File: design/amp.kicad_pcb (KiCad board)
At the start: 2 copper layers, 61 x 36 mm, 59 parts, among them IC1 CP2102N-A02-GQFN24R, IC2 STM6601CQ2BDM6F, IC3 LD39200PU33R, J1 USB4105-GF-A, J2 SM04B-SRSS-TB(LF)(SN), J3 Conn_01x02_Female, J4 Conn_02x03_Odd_Even, J5 SM04B-SRSS-TB(LF)(SN), J6 SM04B-SRSS-TB(LF)(SN), J7 SM04B-SRSS-TB(LF)(SN), Q1 PMBT2222,215, Q2 PMBT2222,215, Q3 Si2347DS-T1-GE3, U1 ESP32-WROOM-32D, U2 LIS2HH12

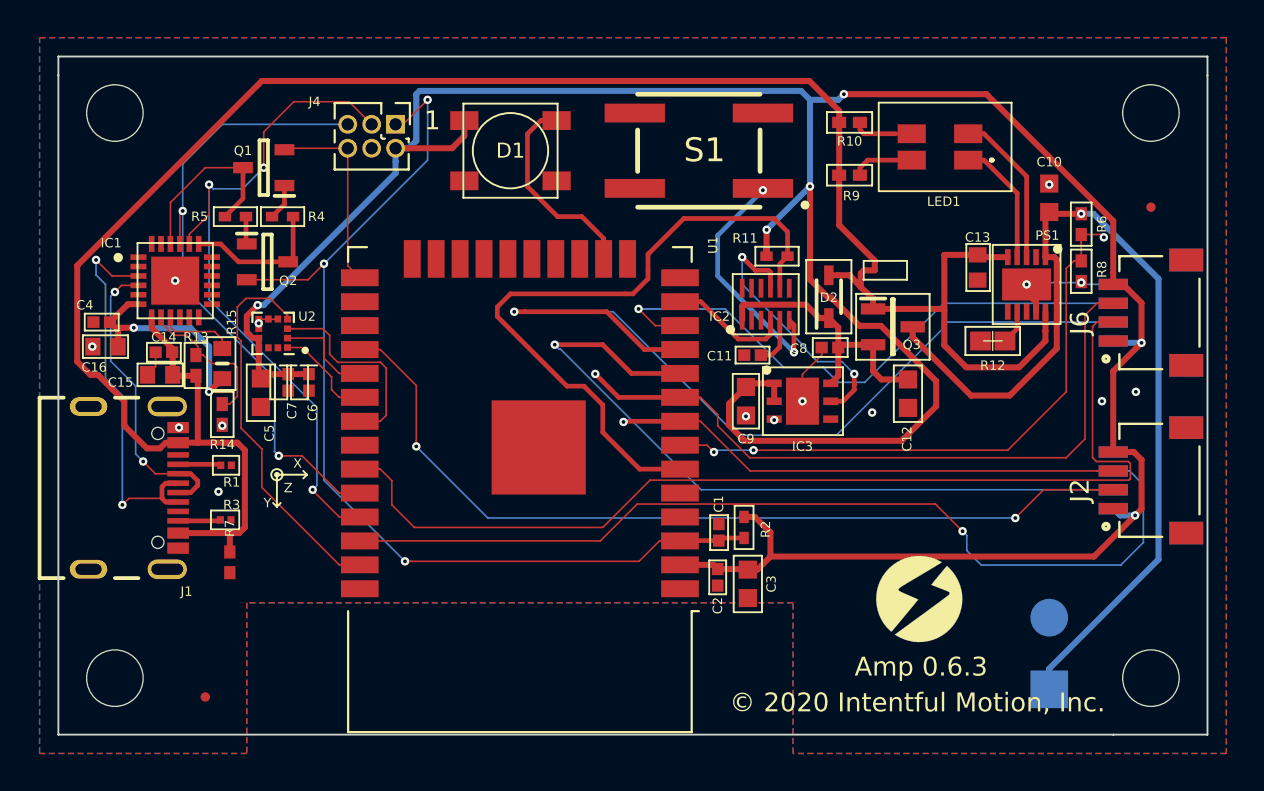
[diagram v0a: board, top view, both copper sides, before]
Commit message: moved components to fit all connectors on the top layer
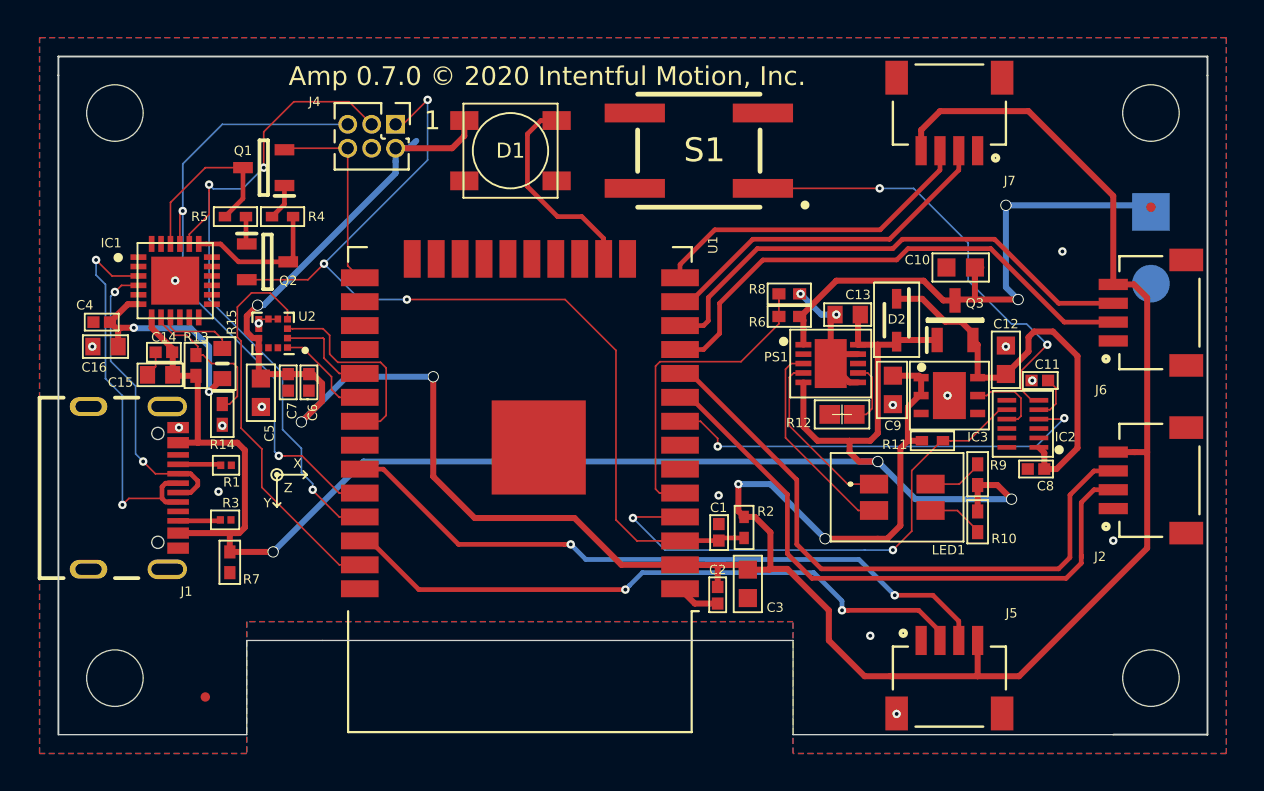
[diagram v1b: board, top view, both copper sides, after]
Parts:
- removed the G*** at (100.7, 60.8)
- J5, J7: moved to F.Cu
- moved J3 25.9 mm to (113.0, 40.2), turned to 270 degrees
- moved R10 22.3 mm to (103.8, 56.7), turned to 90 degrees
- moved LED1 18.7 mm to (99.8, 55.4), turned to 0 degrees
- moved R9 17.3 mm to (103.8, 54.2), turned to 270 degrees
- moved R6 16.3 mm to (93.8, 45.8), turned to 0 degrees
- moved R8 15.5 mm to (93.8, 44.6), turned to 0 degrees
- moved C11 15.3 mm to (107.1, 49.2)
- moved IC2 15.1 mm to (106.2, 51.5), turned to 180 degrees
- moved R11 12.8 mm to (101.4, 52.4)
- moved C8 12.7 mm to (106.9, 53.9)
- moved J7 12.2 mm to (102.3, 37.0), turned to 180 degrees
- moved J5 12.2 mm to (102.3, 63.0), turned to 0 degrees
- moved PS1 11.2 mm to (96.0, 48.3), turned to 0 degrees
- moved R12 8.90 mm to (96.6, 51.0)
- moved C9 7.82 mm to (99.3, 49.7)
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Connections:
- net Net-(C11-Pad1) renamed /DEBOUNCE
- net Net-(C12-Pad2) renamed /V_FILTERED
- net Net-(IC2-Pad9) renamed /POWER_ENABLE
- net Net-(LED1-Pad1) renamed /CHRG
- net Net-(LED1-Pad2) renamed /V_CHRG
- net Net-(LED1-Pad3) renamed /DONE
- net Net-(LED1-Pad4) renamed /V_DONE
- J2 pad 2: /LED1_CLK -> /LED2_CLK
- J2 pad 3: /LED1_DATA -> /LED2_DATA
- J5 pad 2: /LED3_CLK -> /LED1_CLK
- J5 pad 3: /LED3_DATA -> /LED1_DATA
- J6 pad 2: /LED2_CLK -> /LED3_CLK
- J6 pad 3: /LED2_DATA -> /LED3_DATA
- U1 pad 10: /LED3_DATA -> /LED2_DATA
- U1 pad 11: /LED4_DATA -> /LED3_CLK
- U1 pad 12: /LED4_CLK -> /LED3_DATA
- U1 pad 13: /AMP_PWR_HLD -> /LED4_CLK
- U1 pad 14: (no net) -> /LED4_DATA
- U1 pad 28: /LED1_CLK -> (no net)
- U1 pad 33: /LED2_CLK -> /LED1_DATA
- U1 pad 36: /LED3_CLK -> /LED1_CLK
- U1 pad 4: (no net) -> /AMP_INPUT
- U1 pad 5: (no net) -> /VBAT_SENSE
- U1 pad 6: /AMP_INPUT -> (no net)
- U1 pad 7: /VBAT_SENSE -> (no net)
- U1 pad 8: /LED1_DATA -> /AMP_PWR_HLD
- U1 pad 9: /LED2_DATA -> /LED2_CLK
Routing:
- net /LED4_DATA: track 46.9 -> 17.6 mm, vias 1 -> 0
- net /VBUS: track 114.3 -> 89.2 mm, vias 0 -> 3
- net /LED2_CLK: track 55.1 -> 32.8 mm
- net /LED3_CLK: track 49.7 -> 27.8 mm, vias 1 -> 0
- net /VBAT: track 49.8 -> 30.3 mm, vias 1 -> 2
- net /AMP_PWR_HLD: track 6.48 -> 23.1 mm, vias 0 -> 2
- net /LED4_CLK: track 35.1 -> 18.7 mm, vias 1 -> 0
- net /VBAT_SENSE: track 32.1 -> 17.0 mm, vias 3 -> 0
- net /LED3_DATA: track 40.1 -> 27.0 mm, vias 1 -> 0
- net /LED1_CLK: track 47.1 -> 34.3 mm
- net /PB_INPUT: track 13.1 -> 23.9 mm
- net /POWER_ENABLE: track 14.7 -> 4.29 mm, vias 2 -> 0
- net /LED1_DATA: track 27.1 -> 36.2 mm, vias 1 -> 2
- net /V_FILTERED: track 14.9 -> 23.3 mm
- net /AMP_INPUT: track 36.0 -> 28.0 mm, vias 0 -> 2
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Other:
- outline, holes or cut-outs redrawn
- net class Power: via_dia 0.45 -> 0.6; via_drill 0.2 -> 0.5
- board text added: "+"
- board text added: "Amp 0.7.0 © 2020 Intentful Motion, Inc."
- board text removed: "Amp 0.6.3"
- board text removed: "© 2020 Intentful Motion, Inc."

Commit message: removed bicolor led for charge and done. inputs redirected to ESP32
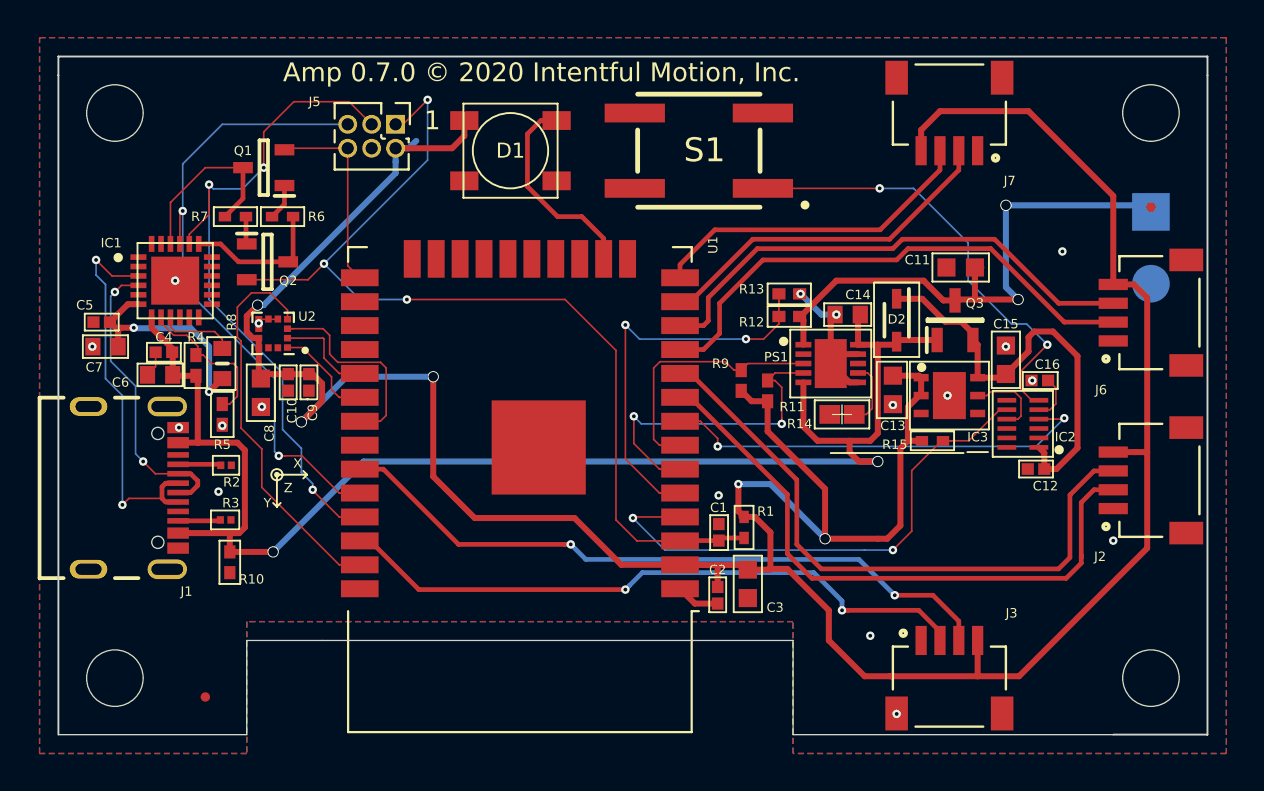
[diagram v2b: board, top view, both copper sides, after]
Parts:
- removed LED1: IN-S128DATRG, SamacSys_Parts:INS128DATRG
- C10, C12, C5, C9: value GRM188R61A106KE69D -> GRM155R61H104KE14D; footprint GRM188R61A106KE69D:CAPC1608X95N -> SamacSys_Parts:CAPC1005X55N
- C11, C8: value GRM155R61H104KE14D -> GRM188R61A106KE69D; footprint SamacSys_Parts:CAPC1005X55N -> GRM188R61A106KE69D:CAPC1608X95N
- C13, C15: value TMK107BJ105KA-T -> GRM188R61A106KE69D; footprint SamacSys_Parts:CAPC1608X90N -> GRM188R61A106KE69D:CAPC1608X95N
- C14, C6, C7: value GRM155R61H104KE14D -> TMK107BJ105KA-T; footprint SamacSys_Parts:CAPC1005X55N -> SamacSys_Parts:CAPC1608X90N
- C16: value TMK107BJ105KA-T -> GRM155R61H104KE14D; footprint SamacSys_Parts:CAPC1608X90N -> SamacSys_Parts:CAPC1005X55N
- J3: value Conn_01x02_Female -> SM04B-SRSS-TB(LF)(SN); footprint Connector_Wire:SolderWirePad_1x02_P3.81mm_Drill0.8mm -> SM04B-SRSS-TB_LF__SN_:JST_SM04B-SRSS-TB(LF)(SN); moved to F.Cu
- J4: value Conn_02x03_Odd_Even -> Conn_01x02_Female; footprint Connector_PinHeader_1.27mm:PinHeader_2x03_P1.27mm_Vertical -> Connector_Wire:SolderWirePad_1x02_P3.81mm_Drill0.8mm; moved to B.Cu
- J5: value SM04B-SRSS-TB(LF)(SN) -> Conn_02x03_Odd_Even; footprint SM04B-SRSS-TB_LF__SN_:JST_SM04B-SRSS-TB(LF)(SN) -> Connector_PinHeader_1.27mm:PinHeader_2x03_P1.27mm_Vertical
- R1: value RC0201FR-075K1L -> RC0402FR-0710KL; footprint RC0201FR-075K1L:RESC0603X26N -> footprints:RC0402FR-0710KL
- R10: value CRCW0402140RFKEDC -> AC0402FR-13100KL-SamacSys_Parts; footprint SamacSys_Parts:RESC1005X35N -> SamacSys_Parts:RESC1005X37N
- R11: footprint footprints:RC0402FR-0710KL -> SamacSys_Parts:RESC1005X40N
- R12: value RC0603FR-101K2L -> AC0402FR-13100KL; footprint SamacSys_Parts:RESC1608X55N -> SamacSys_Parts:RESC1005X37N
- R13: value CRCW0402140RFKEDC -> AC0402FR-13100KL; footprint SamacSys_Parts:RESC1005X35N -> SamacSys_Parts:RESC1005X37N
- R14: value CRCW0402140RFKEDC -> RC0603FR-101K2L; footprint SamacSys_Parts:RESC1005X35N -> SamacSys_Parts:RESC1608X55N
- R15: value RC0603FR-101K2L -> RC0402FR-0710KL; footprint SamacSys_Parts:RESC1608X55N -> footprints:RC0402FR-0710KL
- R2: value RC0402FR-0710KL -> RC0201FR-075K1L; footprint footprints:RC0402FR-0710KL -> RC0201FR-075K1L:RESC0603X26N
- R4, R5: value RC0402FR-0710KL -> CRCW0402140RFKEDC; footprint footprints:RC0402FR-0710KL -> SamacSys_Parts:RESC1005X35N
- R6: value AC0402FR-13100KL -> RC0402FR-0710KL; footprint SamacSys_Parts:RESC1005X37N -> footprints:RC0402FR-0710KL
- R7: value AC0402FR-13100KL-SamacSys_Parts -> RC0402FR-0710KL; footprint SamacSys_Parts:RESC1005X37N -> footprints:RC0402FR-0710KL
- R8: value AC0402FR-13100KL -> RC0603FR-101K2L; footprint SamacSys_Parts:RESC1005X37N -> SamacSys_Parts:RESC1608X55N
- R9: value CRCW0402140RFKEDC -> RC0402FR-0710KL; footprint SamacSys_Parts:RESC1005X35N -> SamacSys_Parts:RESC1005X40N
- moved C16 49.6 mm to (107.1, 49.2)
- moved C15 44.9 mm to (105.3, 48.1), turned to 270 degrees
- moved C8 41.3 mm to (65.8, 49.9), turned to 270 degrees
- moved J4 40.4 mm to (113.0, 40.2)
- moved J5 40.2 mm to (72.9, 35.6), turned to 270 degrees
- moved R10 39.8 mm to (64.1, 58.9), turned to 270 degrees
- moved R15 37.9 mm to (101.4, 52.4), turned to 180 degrees
- moved C14 36.4 mm to (96.9, 45.7)
- moved C10 36.2 mm to (67.2, 49.3), turned to 270 degrees
- moved R14 32.9 mm to (96.6, 51.0), turned to 180 degrees
- moved R13 31.7 mm to (93.8, 44.6), turned to 0 degrees
- moved C9 31.0 mm to (68.3, 49.3), turned to 270 degrees
- moved R8 30.3 mm to (63.7, 48.3), turned to 270 degrees
- moved R1 27.7 mm to (91.4, 57.0), turned to 90 degrees
- moved R2 27.7 mm to (63.9, 53.7), turned to 180 degrees
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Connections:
- C10 pad 1: GND -> +3V3
- C10 pad 2: /VBAT -> GND
- C11 pad 1: /DEBOUNCE -> GND
- C11 pad 2: GND -> /VBAT
- C13 pad 1: /VBUS -> GND
- C13 pad 2: GND -> +3V3
- C15 pad 1: /VBUS -> GND
- C15 pad 2: GND -> /V_FILTERED
- C16 pad 1: /UART_VDD -> /DEBOUNCE
- C4 pad 1: /UART_VDD -> /VBUS
- C5 pad 1: +3V3 -> /UART_VDD
- C6 pad 1: +3V3 -> /VBUS
- C7 pad 1: +3V3 -> /UART_VDD
- C8 pad 1: GND -> +3V3
- C8 pad 2: /V_FILTERED -> GND
- C9 pad 1: GND -> +3V3
- C9 pad 2: +3V3 -> GND
- J3 pad 1: /VBAT -> GND
- J3 pad 2: GND -> /LED1_CLK
- J4 pad 1: /RESET -> /VBAT
- J4 pad 2: +3V3 -> GND
- J5 pad 1: GND -> /RESET
- J5 pad 2: /LED1_CLK -> +3V3
- J5 pad 3: /LED1_DATA -> /TXD0
- J5 pad 4: +3V3 -> GND
- R1 pad 1: GND -> /RESET
- R1 pad 2: Net-(J1-PadA5) -> +3V3
- R10 pad 1: /V_DONE -> /VBUS
- R10 pad 2: /VBUS -> GND
- R11 pad 1: /AMP_INPUT -> +3V3
- R11 pad 2: +3V3 -> /CHRG
- R12 pad 1: Net-(PS1-Pad7) -> /VBAT_SENSE
- R12 pad 2: GND -> /VBAT
- R13 pad 1: /VBUS -> /VBAT_SENSE
- R13 pad 2: Net-(IC1-Pad8) -> GND
- R14 pad 1: Net-(IC1-Pad8) -> Net-(PS1-Pad7)
- R15 pad 1: Net-(IC1-Pad9) -> /AMP_INPUT
- R15 pad 2: /UART_VDD -> +3V3
- R2 pad 1: /RESET -> GND
- R2 pad 2: +3V3 -> Net-(J1-PadA5)
- R4 pad 1: Net-(Q1-Pad1) -> /VBUS
- R4 pad 2: /RTS -> Net-(IC1-Pad8)
- R5 pad 1: Net-(Q2-Pad1) -> Net-(IC1-Pad8)
- R5 pad 2: /DTR -> GND
- R6 pad 1: /VBAT_SENSE -> Net-(Q1-Pad1)
- R6 pad 2: /VBAT -> /RTS
- R7 pad 1: /VBUS -> Net-(Q2-Pad1)
- R7 pad 2: GND -> /DTR
- R8 pad 1: /VBAT_SENSE -> Net-(IC1-Pad9)
- R8 pad 2: GND -> /UART_VDD
- R9 pad 1: /V_CHRG -> +3V3
- R9 pad 2: /VBUS -> /DONE
- U1 pad 6: (no net) -> /CHRG
- U1 pad 7: (no net) -> /DONE
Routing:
- net /VBUS: track 89.2 -> 77.8 mm, vias 3 -> 2
- net +3V3: track 154.0 -> 164.1 mm
- net /CHRG: track 9.20 -> 17.4 mm, vias 0 -> 2
- net /VBAT_SENSE: track 17.0 -> 21.1 mm, vias 0 -> 2
- net /V_CHRG: track 2.98 -> 0.00 mm
- net /V_DONE: track 2.95 -> 0.00 mm
- net /DONE: track 11.0 -> 13.7 mm
